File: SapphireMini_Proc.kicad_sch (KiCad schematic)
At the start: 38 parts, among them J801 USB_B_Micro, J802 Conn_02x05_Odd_Even, J803 Conn_02x05_Odd_Even, J805 Conn_01x04_Male, SW701 EVQP7C01P, SW801 EVQP7C01P, U801 ATSAMD21G18A-A

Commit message: Added optional RSCK footprint
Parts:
- C805, C808: Attrition (none) -> 0
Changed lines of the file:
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@@
+      (effects (font (size 1.27 1.27)) hide)
+    )
+    (property "Attrition" "0" (id 9) (at 109.22 58.42 0)
       (effects (font (size 1.27 1.27)) hide)
     )
@@
       (effects (font (size 1.27 1.27)) hide)
     )
+    (property "Attrition" "0" (id 9) (at 83.82 57.15 0)
+      (effects (font (size 1.27 1.27)) hide)
+    )

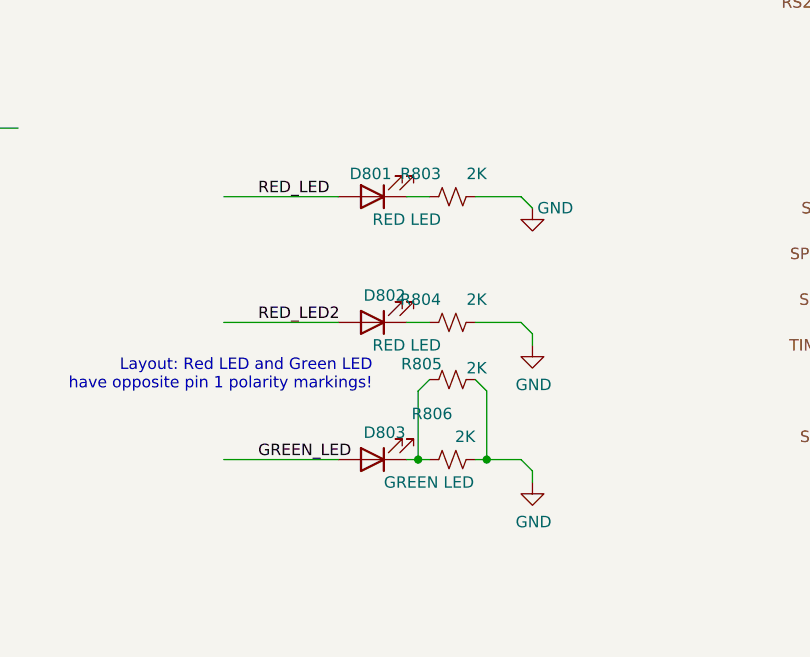
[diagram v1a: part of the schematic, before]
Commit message: Updated PCB comments
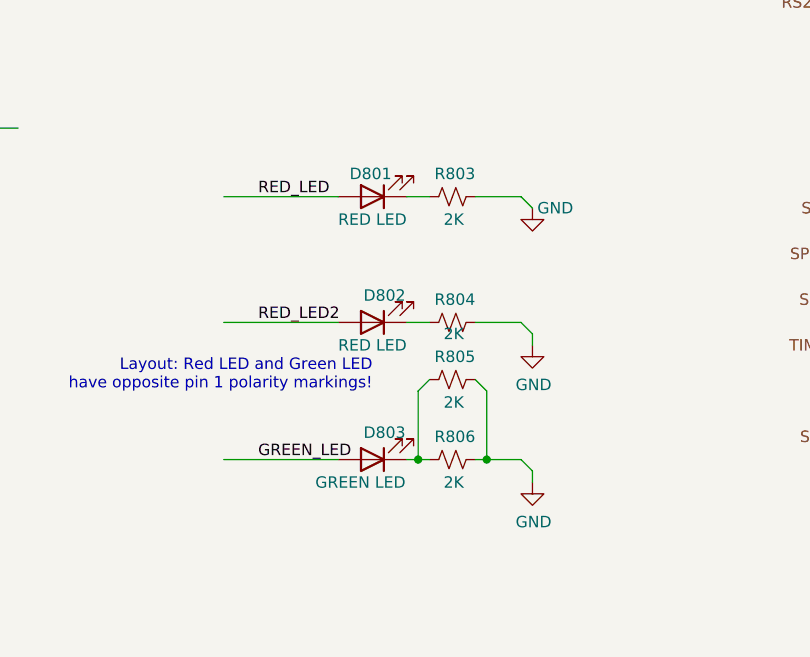
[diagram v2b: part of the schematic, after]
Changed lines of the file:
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@@
       (effects (font (size 1.27 1.27)) (justify right))
     )
-    (property "Value" "RED LED" (id 1) (at 287.02 91.44 0)
+    (property "Value" "RED LED" (id 1) (at 283.21 91.44 0)
       (effects (font (size 1.27 1.27)) (justify right))
     )
@@
   (symbol (lib_id "Device:R_Small_US") (at 295.91 88.9 90) (unit 1)
     (in_bom yes) (on_board yes)
-    (property "Reference" "R803" (id 0) (at 294.64 86.36 90)
-      (effects (font (size 1.27 1.27)) (justify left))
-    )
-    (property "Value" "2K" (id 1) (at 299.72 86.36 90)
+    (property "Reference" "R803" (id 0) (at 298.45 86.36 90)
+      (effects (font (size 1.27 1.27)) (justify left))
+    )
+    (property "Value" "2K" (id 1) (at 297.18 91.44 90)
       (effects (font (size 1.27 1.27)) (justify left))
     )
@@
   (symbol (lib_id "Device:R_Small_US") (at 295.91 102.87 90) (unit 1)
     (in_bom yes) (on_board yes)
-    (property "Reference" "R804" (id 0) (at 294.64 100.33 90)
-      (effects (font (size 1.27 1.27)) (justify left))
-    )
-    (property "Value" "2K" (id 1) (at 299.72 100.33 90)
+    (property "Reference" "R804" (id 0) (at 298.45 100.33 90)
+      (effects (font (size 1.27 1.27)) (justify left))
+    )
+    (property "Value" "2K" (id 1) (at 297.18 104.14 90)
       (effects (font (size 1.27 1.27)) (justify left))
     )
@@
       (effects (font (size 1.27 1.27)) (justify right))
     )
-    (property "Value" "RED LED" (id 1) (at 287.02 105.41 0)
+    (property "Value" "RED LED" (id 1) (at 283.21 105.41 0)
       (effects (font (size 1.27 1.27)) (justify right))
     )
@@
   (symbol (lib_id "Device:R_Small_US") (at 295.91 109.22 90) (unit 1)
     (in_bom yes) (on_board yes)
-    (property "Reference" "R805" (id 0) (at 294.7416 107.4928 90)
-      (effects (font (size 1.27 1.27)) (justify left))
-    )
-    (property "Value" "2K" (id 1) (at 299.72 107.95 90)
+    (property "Reference" "R805" (id 0) (at 298.45 106.68 90)
+      (effects (font (size 1.27 1.27)) (justify left))
+    )
+    (property "Value" "2K" (id 1) (at 297.18 111.76 90)
       (effects (font (size 1.27 1.27)) (justify left))
     )
@@
   (symbol (lib_id "Device:R_Small_US") (at 295.91 118.11 90) (unit 1)
     (in_bom yes) (on_board yes)
-    (property "Reference" "R806" (id 0) (at 295.91 113.03 90)
-      (effects (font (size 1.27 1.27)) (justify left))
-    )
-    (property "Value" "2K" (id 1) (at 298.45 115.57 90)
+    (property "Reference" "R806" (id 0) (at 298.45 115.57 90)
+      (effects (font (size 1.27 1.27)) (justify left))
+    )
+    (property "Value" "2K" (id 1) (at 297.18 120.65 90)
       (effects (font (size 1.27 1.27)) (justify left))
     )
@@
       (effects (font (size 1.27 1.27)) (justify right))
     )
-    (property "Value" "GREEN LED" (id 1) (at 288.29 120.65 0)
-      (effects (font (size 1.27 1.27)) (justify right))
-    )
+    (property "Value" "GREEN LED" (id 1) (at 280.67 120.65 0)
+      (effects (font (size 1.27 1.27)) (justify right))
+    )

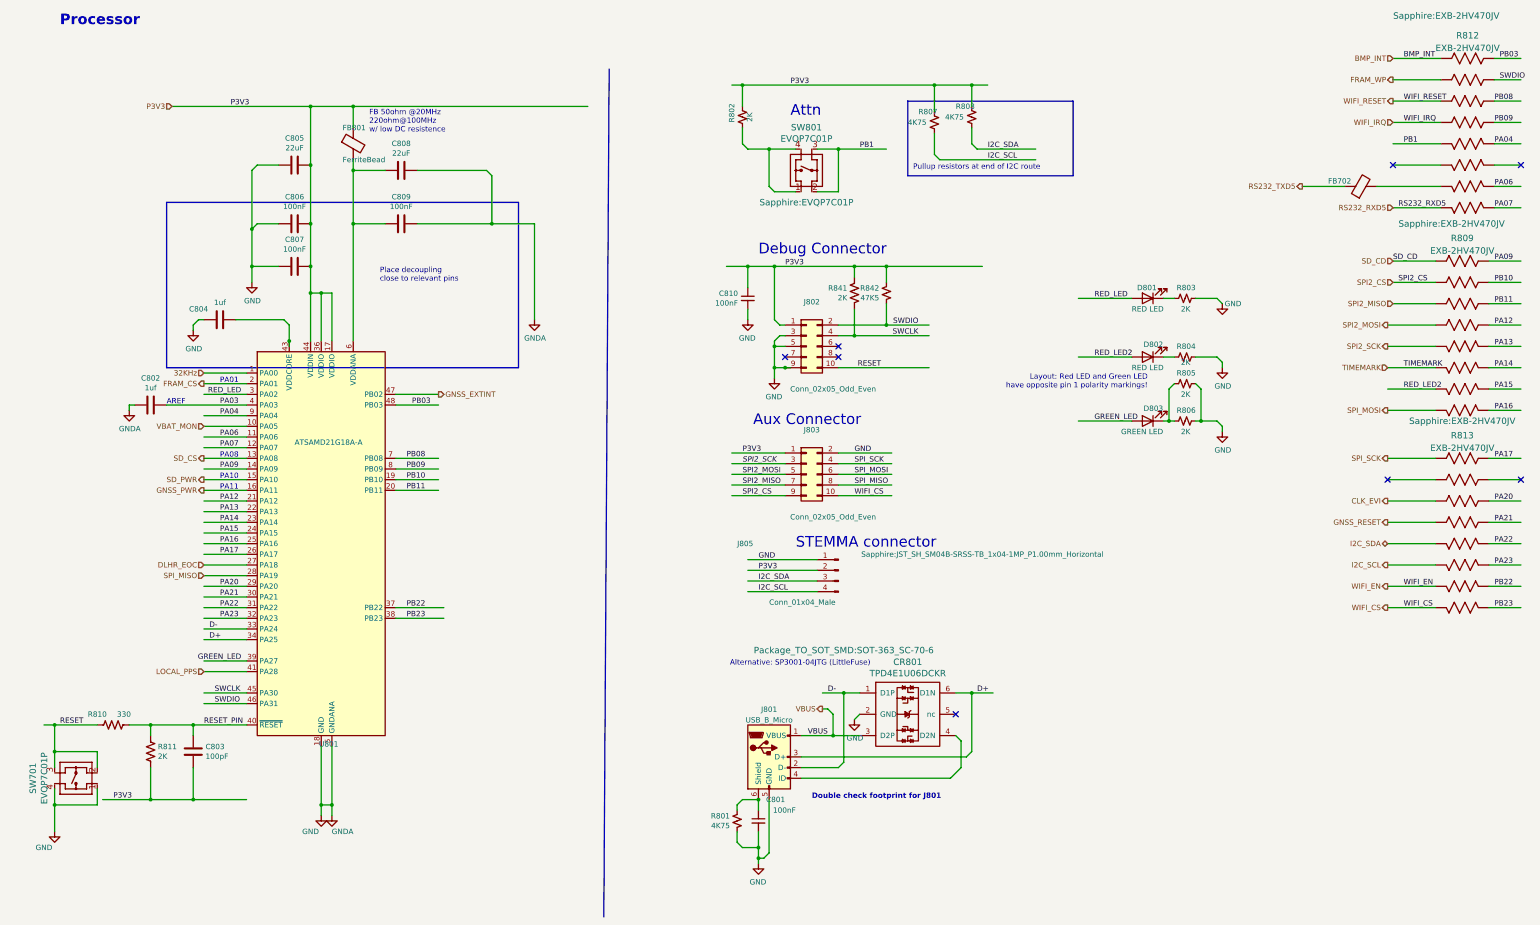
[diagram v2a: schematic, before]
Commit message: Updated to fix noted problems
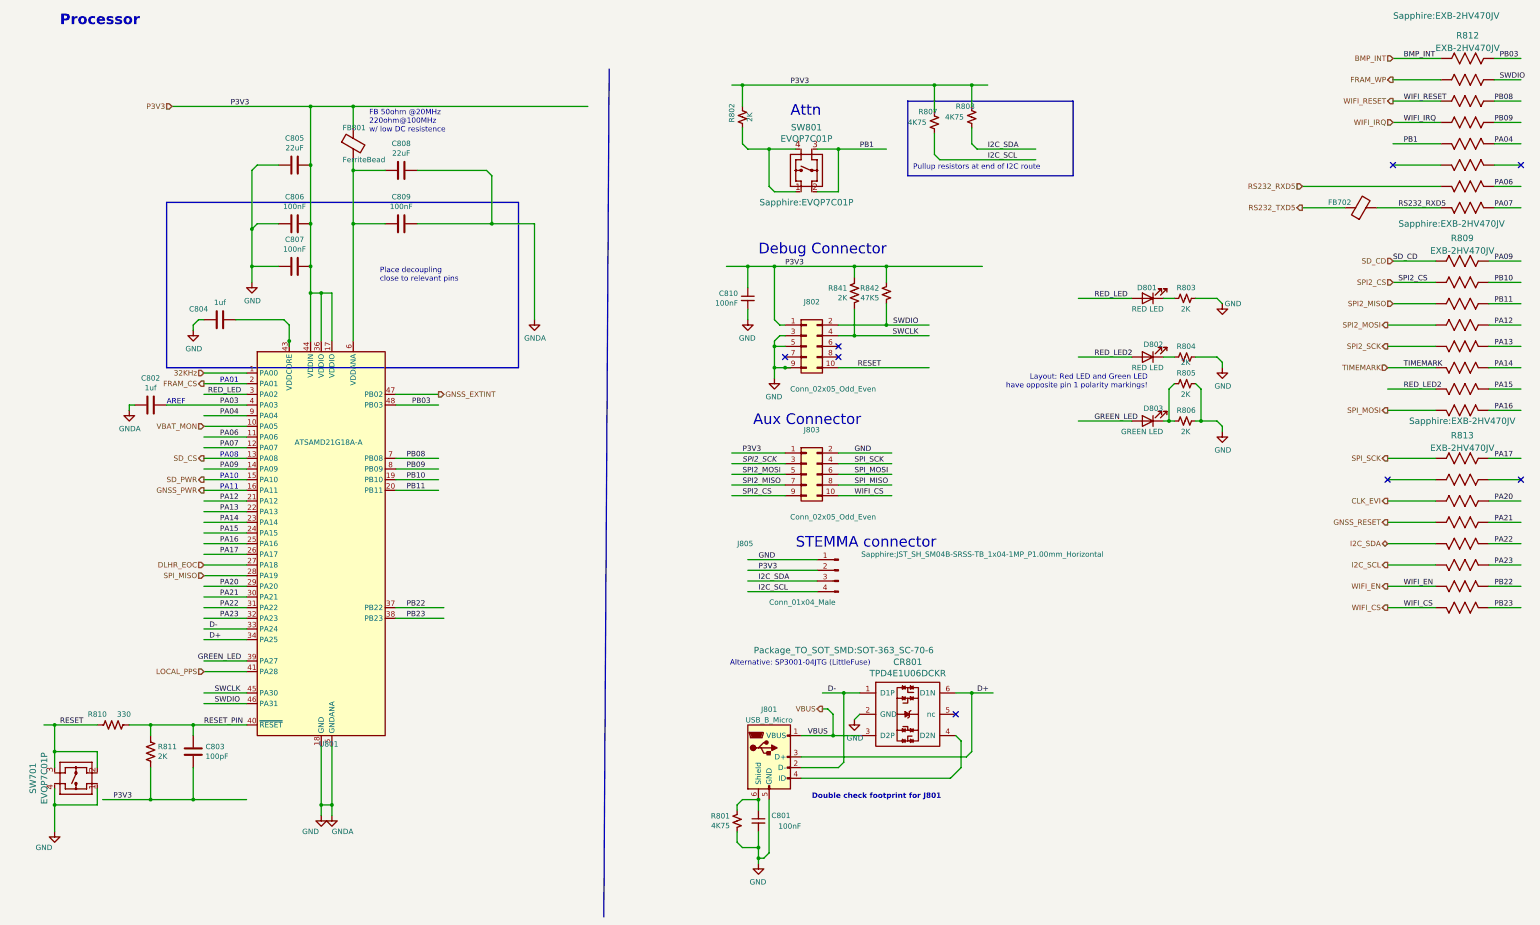
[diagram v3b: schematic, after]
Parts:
- J801: footprint SapphineMinimal:uUSB_B -> SapphineMinimal:FCI_10118193-0001LF
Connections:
- net RS232_RXD5: now also FB702.2, R812.7
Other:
- moved on the sheet: FB702
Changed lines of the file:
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@@
+    (stroke (width 0) (type default) (color 0 0 0 0))
+  )
+  (wire (pts (xy 334.01 67.31) (xy 323.85 67.31))
     (stroke (width 0) (type default) (color 0 0 0 0))
   )
@@
     (stroke (width 0) (type default) (color 0 0 0 0))
   )
-  (wire (pts (xy 345.44 67.31) (xy 356.87 67.31))
+  (wire (pts (xy 341.63 67.31) (xy 356.87 67.31))
     (stroke (width 0) (type default) (color 0 0 0 0))
   )
@@
     (stroke (width 0) (type default) (color 0 0 0 0))
   )
-  (wire (pts (xy 341.63 62.23) (xy 356.87 62.23))
+  (wire (pts (xy 323.85 62.23) (xy 356.87 62.23))
     (stroke (width 0) (type default) (color 0 0 0 0))
   )
@@
   )
   (wire (pts (xy 44.45 114.3) (xy 45.72 114.3))
-    (stroke (width 0) (type default) (color 0 0 0 0))
-  )
-  (wire (pts (xy 323.85 62.23) (xy 334.01 62.23))
     (stroke (width 0) (type default) (color 0 0 0 0))
   )
@@
     (effects (font (size 1.27 1.27)) (justify right))
   )
-  (hierarchical_label "RS232_TXD5" (shape output) (at 323.85 62.23 180)
+  (hierarchical_label "RS232_TXD5" (shape output) (at 323.85 67.31 180)
     (effects (font (size 1.27 1.27)) (justify right))
   )
@@
     (effects (font (size 1.27 1.27)) (justify right))
   )
-  (hierarchical_label "RS232_RXD5" (shape input) (at 345.44 67.31 180)
+  (hierarchical_label "RS232_RXD5" (shape input) (at 323.85 62.23 180)
     (effects (font (size 1.27 1.27)) (justify right))
   )
@@
   (symbol (lib_id "Device:C_Small") (at 194.31 213.36 0) (mirror y) (unit 1)
     (in_bom yes) (on_board yes)
-    (property "Reference" "C801" (id 0) (at 200.66 208.28 0)
+    (property "Reference" "C801" (id 0) (at 201.93 212.09 0)
       (effects (font (size 1.27 1.27)) (justify left))
     )
-    (property "Value" "100nF" (id 1) (at 203.2 210.82 0)
+    (property "Value" "100nF" (id 1) (at 204.47 214.63 0)
       (effects (font (size 1.27 1.27)) (justify left))
     )
@@
     (property "Reference" "J801" (id 0) (at 196.85 186.8002 0))
     (property "Value" "USB_B_Micro" (id 1) (at 196.85 189.3371 0))
-    (property "Footprint" "SapphineMinimal:uUSB_B" (id 2) (at 200.66 199.39 0)
+    (property "Footprint" "SapphineMinimal:FCI_10118193-0001LF" (id 2) (at 200.66 199.39 0)
       (effects (font (size 1.27 1.27)) hide)
     )
@@
     (pin "6")
   )
-  (symbol (lib_id "Device:FerriteBead") (at 337.82 62.23 90) (unit 1)
-    (in_bom yes) (on_board yes)
-    (property "Reference" "FB702" (id 0) (at 332.74 60.96 90))
-    (property "Value" "FerriteBead" (id 1) (at 337.82 63.5 90)
-      (effects (font (size 1.27 1.27)) hide)
-    )
-    (property "Footprint" "Inductor_SMD:L_0603_1608Metric" (id 2) (at 337.82 64.008 90)
-      (effects (font (size 1.27 1.27)) hide)
-    )
-    (property "Datasheet" "~" (id 3) (at 337.82 62.23 0)
-      (effects (font (size 1.27 1.27)) hide)
-    )
-    (property "Description" "220 Ohms @ 100 MHz 1 Ferrite Bead 0603 (1608 Metric) 500mA 250mOhm" (id 4) (at 337.82 62.23 0)
-      (effects (font (size 1.27 1.27)) hide)
-    )
-    (property "MPN" "BLM18AG221SN1D" (id 5) (at 337.82 62.23 0)
-      (effects (font (size 1.27 1.27)) hide)
-    )
+  (symbol (lib_id "Device:FerriteBead") (at 337.82 67.31 90) (unit 1)
+    (in_bom yes) (on_board yes)
+    (property "Reference" "FB702" (id 0) (at 332.74 66.04 90))
+    (property "Value" "FerriteBead" (id 1) (at 337.82 68.58 90)
+      (effects (font (size 1.27 1.27)) hide)
+    )
+    (property "Footprint" "Inductor_SMD:L_0603_1608Metric" (id 2) (at 337.82 69.088 90)
+      (effects (font (size 1.27 1.27)) hide)
+    )
+    (property "Datasheet" "~" (id 3) (at 337.82 67.31 0)
+      (effects (font (size 1.27 1.27)) hide)
+    )
+    (property "Description" "220 Ohms @ 100 MHz 1 Ferrite Bead 0603 (1608 Metric) 500mA 250mOhm" (id 4) (at 337.82 67.31 0)
+      (effects (font (size 1.27 1.27)) hide)
+    )
+    (property "MPN" "BLM18AG221SN1D" (id 5) (at 337.82 67.31 0)
+      (effects (font (size 1.27 1.27)) hide)
+    )

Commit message: InProgress
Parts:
- J802: footprint Connector_PinHeader_1.27mm:PinHeader_2x05_P1.27mm_Vertical -> SapphineMinimal:CONN_3220-10-0100-00_CNC
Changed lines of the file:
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@@
     (property "Reference" "J802" (id 0) (at 207.01 89.7382 0))
     (property "Value" "Conn_02x05_Odd_Even" (id 1) (at 212.09 110.49 0))
-    (property "Footprint" "Connector_PinHeader_1.27mm:PinHeader_2x05_P1.27mm_Vertical" (id 2) (at 205.74 100.33 0)
+    (property "Footprint" "SapphineMinimal:CONN_3220-10-0100-00_CNC" (id 2) (at 205.74 100.33 0)
       (effects (font (size 1.27 1.27)) hide)
     )

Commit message: M2R2 basic DRC passed
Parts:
- J802: footprint SapphineMinimal:CONN_3220-10-0100-00_CNC -> Sapphire:3220-10-0100-00
- J803: footprint Connector_PinHeader_1.27mm:PinHeader_2x05_P1.27mm_Vertical -> Sapphire:3220-10-0100-00
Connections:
- net RS232_RXD5: no longer FB702.2, R812.8
- net at C801.1, R801.2: now also J801.S1 (Shield); no longer J801.6 (Shield)
- new net: FB702.2, R812.8
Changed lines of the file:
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@@
-    (effects (font (size 1.27 1.27)) (justify left bottom))
-  )
-  (label "RS232_RXD5" (at 346.71 67.31 0)
     (effects (font (size 1.27 1.27)) (justify left bottom))
   )
@@
     (property "Reference" "J802" (id 0) (at 207.01 89.7382 0))
     (property "Value" "Conn_02x05_Odd_Even" (id 1) (at 212.09 110.49 0))
-    (property "Footprint" "SapphineMinimal:CONN_3220-10-0100-00_CNC" (id 2) (at 205.74 100.33 0)
+    (property "Footprint" "Sapphire:3220-10-0100-00" (id 2) (at 205.74 100.33 0)
       (effects (font (size 1.27 1.27)) hide)
     )
@@
     (property "Reference" "J803" (id 0) (at 207.01 120.2182 0))
     (property "Value" "Conn_02x05_Odd_Even" (id 1) (at 212.09 140.97 0))
-    (property "Footprint" "Connector_PinHeader_1.27mm:PinHeader_2x05_P1.27mm_Vertical" (id 2) (at 205.74 130.81 0)
+    (property "Footprint" "Sapphire:3220-10-0100-00" (id 2) (at 205.74 130.81 0)
       (effects (font (size 1.27 1.27)) hide)
     )
@@
     (pin "4")
     (pin "5")
-    (pin "6")
+    (pin "S1")
   )
   (symbol (lib_id "Device:FerriteBead") (at 337.82 67.31 90) (unit 1)
